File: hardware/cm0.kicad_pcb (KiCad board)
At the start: 4 copper layers, 100 x 90 mm, 107 parts, among them J1 GPDI_A, J2 USB_C_Receptacle_USB2.0_14P, J3 USB_C_Receptacle_USB2.0_14P, J4 USB_A_Stacked, J5 USB_C_Receptacle_USB2.0_14P, J6 AIPEX-1, J8 RJ45_Hanrun_HR913550A_Horizon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, Q1 BSN20, U1 H3, U10 TPD2EUSB30, U11 SY6280AAC, U12 HUSB237, U13 AW13412HDNR, U14 UCL0524P, U15 UCL0524P, U2 H5TQ4G63EFR, U3 AP6212, U4 SY6280AAC, U5 SY6280AAC, U6 TPD2EUSB30, U7 TPD2EUSB30, U8 SY6280AAC, U9 TPD2EUSB30, Y1 26MHz

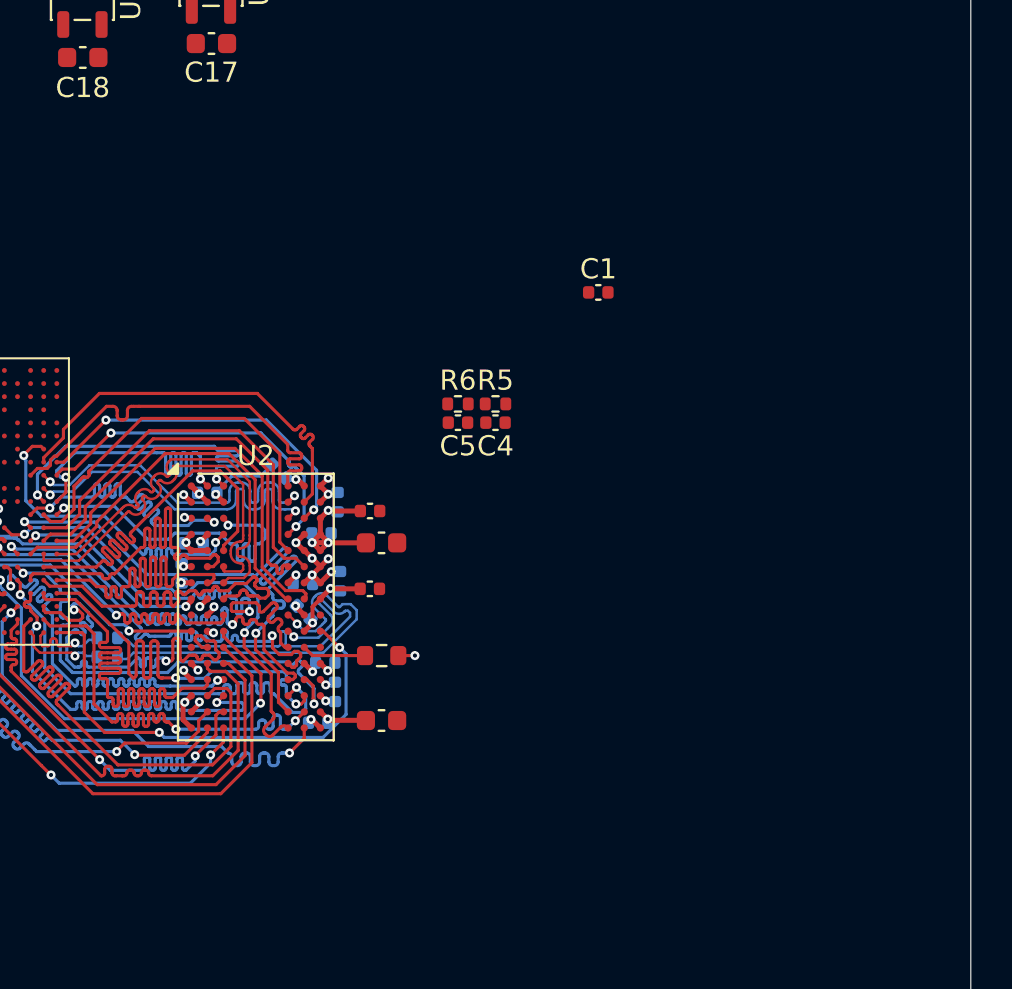
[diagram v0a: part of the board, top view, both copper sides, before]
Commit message: Add eMMC and uSD
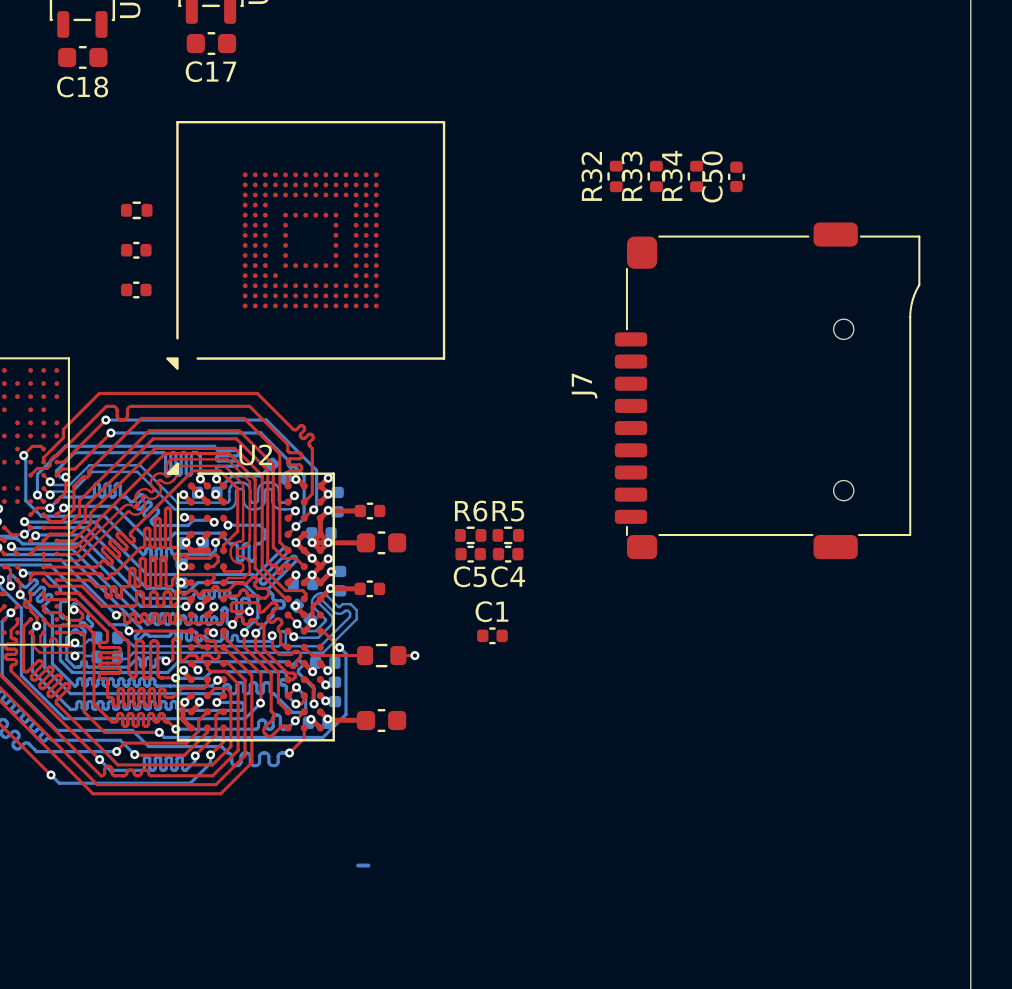
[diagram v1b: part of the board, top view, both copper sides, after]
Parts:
- added C48: 1uF, Capacitor_SMD:C_0402_1005Metric, F.Cu at (111.7, 96.1)
- added C49: 100nF, Capacitor_SMD:C_0402_1005Metric, F.Cu at (111.7, 98.1)
- added C50: 1uF, Capacitor_SMD:C_0402_1005Metric, F.Cu at (141.4, 92.5)
- added J7: Micro_SD_Card_Det1, cm0:microSD_TF-01A, F.Cu at (141.5, 102.8)
- added R31: 10k, Resistor_SMD:R_0402_1005Metric, F.Cu at (111.7, 94.1)
- added R32: 22, Resistor_SMD:R_0402_1005Metric, F.Cu at (135.5, 92.4)
- added R33: 56k, Resistor_SMD:R_0402_1005Metric, F.Cu at (137.5, 92.4)
- added R34: 56k, Resistor_SMD:R_0402_1005Metric, F.Cu at (139.5, 92.4)
- added U16: EMMC5.1_BGA153, Package_BGA:LFBGA-153_11.5x13mm_Layout14x14_P0.5mm, F.Cu at (120.3, 95.6)
- R27: value 6k -> 6.04k
- moved C1 17.8 mm to (129.3, 115.2)
- moved C4 6.55 mm to (130.1, 111.2)
- moved R5 6.55 mm to (130.1, 110.2)
- moved R6 6.55 mm to (128.3, 110.2)
- moved C5 6.55 mm to (128.3, 111.2)
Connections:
- U1 pad A10: (no net) -> unconnected-(U1F-PE1-PadA10)
- U1 pad A11: (no net) -> unconnected-(U1F-PE11-PadA11)
- U1 pad A13: (no net) -> unconnected-(U1F-PA20-PadA13)
- U1 pad A14: (no net) -> unconnected-(U1F-PA21-PadA14)
- U1 pad A16: (no net) -> unconnected-(U1C-PC7-PadA16)
- U1 pad A17: (no net) -> /H3/eMMC_CLK
- U1 pad A19: (no net) -> /H3/SD_D0
- U1 pad A20: (no net) -> unconnected-(U1F-PD4-PadA20)
- U1 pad B10: (no net) -> unconnected-(U1F-PE0-PadB10)
- U1 pad B11: (no net) -> unconnected-(U1F-PE2-PadB11)
- U1 pad B12: (no net) -> unconnected-(U1F-PE12-PadB12)
- U1 pad B13: (no net) -> unconnected-(U1F-PA18-PadB13)
- U1 pad B14: (no net) -> unconnected-(U1F-PA19-PadB14)
- U1 pad B15: (no net) -> unconnected-(U1C-PC3-PadB15)
- U1 pad B16: (no net) -> unconnected-(U1C-PC2-PadB16)
- U1 pad B17: (no net) -> /H3/eMMC_D4
- U1 pad B18: (no net) -> /H3/eMMC_D0
- U1 pad B19: (no net) -> /H3/eMMC_D5
- U1 pad B20: (no net) -> unconnected-(U1F-PD2-PadB20)
- U1 pad B21: (no net) -> unconnected-(U1F-PD6-PadB21)
- U1 pad C10: (no net) -> unconnected-(U1F-PE3-PadC10)
- U1 pad C11: (no net) -> unconnected-(U1F-PE8-PadC11)
- U1 pad C12: (no net) -> unconnected-(U1F-PE9-PadC12)
- U1 pad C13: (no net) -> unconnected-(U1F-PA12-PadC13)
- U1 pad C14: (no net) -> unconnected-(U1F-PA17-PadC14)
- U1 pad C15: (no net) -> unconnected-(U1C-PC0-PadC15)
- U1 pad C16: (no net) -> unconnected-(U1C-PC1-PadC16)
- U1 pad C17: (no net) -> /H3/eMMC_D1
- U1 pad C18: (no net) -> /H3/eMMC_D3
- U1 pad C19: (no net) -> /H3/eMMC_D7
- U1 pad C20: (no net) -> /H3/SD_D2
- U1 pad C21: (no net) -> unconnected-(U1F-PD0-PadC21)
- U1 pad C5: (no net) -> unconnected-(U1F-PE15-PadC5)
- U1 pad C6: (no net) -> unconnected-(U1F-PE14-PadC6)
- U1 pad C7: (no net) -> unconnected-(U1F-PE13-PadC7)
- U1 pad C9: (no net) -> unconnected-(U1F-PE4-PadC9)
- U1 pad D10: (no net) -> unconnected-(U1F-PE6-PadD10)
- U1 pad D11: (no net) -> unconnected-(U1F-PA0-PadD11)
- U1 pad D13: (no net) -> unconnected-(U1F-PA9-PadD13)
- U1 pad D15: (no net) -> unconnected-(U1F-PA16-PadD15)
- U1 pad D17: (no net) -> /H3/eMMC_D2
- U1 pad D19: (no net) -> /H3/SD_D1
- U1 pad D20: (no net) -> /H3/SD_CLK
- U1 pad D5: (no net) -> unconnected-(U1F-PA1-PadD5)
- U1 pad D6: (no net) -> unconnected-(U1F-PA2-PadD6)
- U1 pad D8: (no net) -> unconnected-(U1F-PA7-PadD8)
- U1 pad E10: (no net) -> unconnected-(U1F-PE5-PadE10)
- U1 pad E11: (no net) -> unconnected-(U1F-PA10-PadE11)
- U1 pad E13: (no net) -> unconnected-(U1F-PA3-PadE13)
- U1 pad E14: (no net) -> unconnected-(U1F-PA6-PadE14)
- U1 pad E15: (no net) -> unconnected-(U1F-PA13-PadE15)
- U1 pad E16: (no net) -> /H3/eMMC_CMD
- U1 pad E18: (no net) -> unconnected-(U1F-PD7-PadE18)
- U1 pad E19: (no net) -> unconnected-(U1F-PD12-PadE19)
- U1 pad E20: (no net) -> unconnected-(U1F-PD8-PadE20)
- U1 pad E21: (no net) -> /H3/SD_D3
- U1 pad E8: (no net) -> unconnected-(U1F-PE10-PadE8)
- U1 pad F11: (no net) -> unconnected-(U1F-PA11-PadF11)
- U1 pad F13: (no net) -> unconnected-(U1F-PA8-PadF13)
- U1 pad F14: (no net) -> unconnected-(U1F-PA15-PadF14)
- U1 pad F16: (no net) -> unconnected-(U1C-PC4-PadF16)
- U1 pad F17: (no net) -> /H3/eMMC_D6
- U1 pad F18: (no net) -> /H3/SD_CMD
- U1 pad F19: (no net) -> unconnected-(U1F-PD5-PadF19)
- U1 pad F20: (no net) -> unconnected-(U1F-PD11-PadF20)
- U1 pad F21: (no net) -> unconnected-(U1F-PD9-PadF21)
- U1 pad F5: (no net) -> unconnected-(U1F-PA4-PadF5)
- U1 pad G12: (no net) -> unconnected-(U1F-PA14-PadG12)
- U1 pad G13: (no net) -> VCC-IO
- U1 pad G14: (no net) -> VCC-IO
- U1 pad G15: (no net) -> VCC-IO
- U1 pad G18: (no net) -> /H3/SD_DET
- U1 pad H13: (no net) -> VCC-IO
- U1 pad H14: (no net) -> VCC-IO
- U1 pad H16: (no net) -> /H3/~{eMMC_RST}
- U1 pad H17: (no net) -> unconnected-(U1F-PD1-PadH17)
- U1 pad H18: (no net) -> unconnected-(U1F-PD3-PadH18)
- U1 pad H19: (no net) -> unconnected-(U1F-PD10-PadH19)
- U1 pad H6: (no net) -> unconnected-(U1F-PA5-PadH6)
- U1 pad J14: (no net) -> VCC-IO
- U1 pad J15: (no net) -> +3V3
- U1 pad K17: (no net) -> unconnected-(U1F-PD13-PadK17)
- U1 pad K18: (no net) -> unconnected-(U1F-PD15-PadK18)
- U1 pad K4: (no net) -> unconnected-(U1B-NC-PadK4)
- U1 pad L17: (no net) -> unconnected-(U1F-PD14-PadL17)
- U1 pad L18: (no net) -> unconnected-(U1F-PD16-PadL18)
- U1 pad L19: (no net) -> unconnected-(U1F-PD17-PadL19)
- U1 pad M1: (no net) -> unconnected-(U1F-PL1-PadM1)
- U1 pad M6: (no net) -> unconnected-(U1F-PL9-PadM6)
- U1 pad N1: (no net) -> unconnected-(U1F-PL0-PadN1)
- U1 pad N2: (no net) -> unconnected-(U1F-PL4-PadN2)
- U1 pad P2: (no net) -> unconnected-(U1F-PL2-PadP2)
- U1 pad R1: (no net) -> unconnected-(U1F-PL3-PadR1)
- U1 pad R2: (no net) -> unconnected-(U1F-PL5-PadR2)
- U1 pad T2: (no net) -> unconnected-(U1F-PL8-PadT2)
- U1 pad T3: (no net) -> unconnected-(U1F-PL7-PadT3)
- U1 pad T4: (no net) -> unconnected-(U1F-PL6-PadT4)
- U1 pad U2: (no net) -> unconnected-(U1F-PL11-PadU2)
- U1 pad V2: (no net) -> unconnected-(U1F-PL10-PadV2)
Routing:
- net (no net): track 0.00 -> 0.51 mm
